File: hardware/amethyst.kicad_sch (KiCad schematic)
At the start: 0 parts

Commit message: Layout done
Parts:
- added C1, C2: C, Capacitor_SMD:C_0402_1005Metric, symbol Device:C
- added C10, C11, C12, C13, C14, C3, C4, C5, C6, C7, C8: 100n, Capacitor_SMD:C_0402_1005Metric, symbol Device:C
- added C9: 1u, Capacitor_SMD:C_0402_1005Metric, symbol Device:C
- added J1: Conn_01x02_Pin, Connector_PinHeader_1.00mm:PinHeader_1x02_P1.00mm_Vertical, symbol Connector:Conn_01x02_Pin
- added J2: USB_C_Receptacle_USB2.0_16P, Connector_USB:USB_C_Receptacle_XKB_U262-16XN-4BVC11, symbol Connector:USB_C_Receptacle_USB2.0_16P
- added R1, R2: 5.1k, Resistor_SMD:R_0402_1005Metric, symbol Device:R
- added R3: 1k, Resistor_SMD:R_0402_1005Metric, symbol Device:R
- added R4, R5: 27, Resistor_SMD:R_0402_1005Metric, symbol Device:R
- added U1: RP2040, Package_DFN_QFN:QFN-56-1EP_7x7mm_P0.4mm_EP3.2x3.2mm, symbol MCU_RaspberryPi:RP2040
- added U2: W25Q128JVS, Package_SO:SOIC-8_5.3x5.3mm_P1.27mm, symbol Memory_Flash:W25Q128JVS
- added Y1: Crystal_GND24_Small, Crystal:Crystal_SMD_3225-4Pin_3.2x2.5mm, symbol Device:Crystal_GND24_Small
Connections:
- new net: C2.2, R3.1, Y1.3
- new net: R3.2, U1.21 (XOUT)
- new net: C1.2, U1.20 (XIN), Y1.1
- new net: R4.2, U1.47 (USB_DP)
- new net: J2.A5 (CC1), R2.1
- new net: J2.A4 (VBUS), J2.A9 (VBUS), J2.B4 (VBUS), J2.B9 (VBUS)
- new net: J2.B5 (CC2), R1.1
- new net: J1.1 (Pin_1), U1.26 (RUN)
- new net: R5.2, U1.46 (USB_DM)
- new net +3V3: C10.1, C11.1, C12.1, C13.1, C14.1, C3.1, C4.1, C5.1, C6.1, C7.1, C8.1, C9.1, U1.1 (IOVDD), U1.10 (IOVDD), U1.22 (IOVDD), U1.23 (DVDD), U1.33 (IOVDD), U1.42 (IOVDD), U1.43 (ADC_AVDD), U1.44 (VREG_IN), U1.45 (VREG_VOUT), U1.48 (USB_VDD), U1.49 (IOVDD), U1.50 (DVDD), U2.8 (VCC)
- new net D+: J2.A6 (D+), J2.B6 (D+), R4.1
- new net D-: J2.A7 (D-), J2.B7 (D-), R5.1
- new net GND: C1.1, C10.2, C11.2, C12.2, C13.2, C14.2, C2.1, C3.2, C4.2, C5.2, C6.2, C7.2, C8.2, C9.2, J1.2 (Pin_2), J2.A1 (GND), J2.A12 (GND), J2.B1 (GND), J2.B12 (GND), J2.S1 (SHIELD), R1.2, R2.2, U1.19 (TESTEN), U1.57 (GND), U2.4 (GND), Y1.2, Y1.4
- new net QSPI_SCLK: U1.52 (QSPI_SCLK), U2.6 (CLK)
- new net QSPI_SD0: U1.53 (QSPI_SD0), U2.5 (DI/IO_{0})
- new net QSPI_SD1: U1.55 (QSPI_SD1), U2.2 (DO/IO_{1})
- new net QSPI_SD2: U1.54 (QSPI_SD2), U2.3 (~{WP}/IO_{2})
- new net QSPI_SD3: U1.51 (QSPI_SD3), U2.7 (~{HOLD}/~{RESET}/IO_{3})
- new net QSPI_SS: U1.56 (QSPI_SS), U2.1 (~{CS})
- no-connect marks 0 -> 4

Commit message: PCB Routing
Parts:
- removed C13, C14: 100n, Capacitor_SMD:C_0402_1005Metric, symbol Device:C
- removed J1: Conn_01x02_Pin, Connector_PinHeader_1.00mm:PinHeader_1x02_P1.00mm_Vertical, symbol Connector:Conn_01x02_Pin
- removed R3: 1k, Resistor_SMD:R_0402_1005Metric, symbol Device:R
- removed R4, R5: 27, Resistor_SMD:R_0402_1005Metric, symbol Device:R
- removed U1: RP2040, Package_DFN_QFN:QFN-56-1EP_7x7mm_P0.4mm_EP3.2x3.2mm, symbol MCU_RaspberryPi:RP2040
- removed U2: W25Q128JVS, Package_SO:SOIC-8_5.3x5.3mm_P1.27mm, symbol Memory_Flash:W25Q128JVS
- added U1: nRF52840, Package_DFN_QFN:Nordic_AQFN-73-1EP_7x7mm_P0.5mm, symbol MCU_Nordic:nRF52840
- C10: value 100n -> 100p
- C11, C12: value 100n -> 4.7u
- C9: value 1u -> 100n
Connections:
- net +3V3 is gone; now on net GND: C10.1, C11.1, C12.1, C3.1, C4.1, C5.1, C6.1, C7.1, C8.1, C9.1
- net D+: now also U1.AD6 (D+)
- net D-: now also U1.AD4 (D-)
- net GND: now also U1.B7 (VSS), U1.EP (VSS), U1.F23 (VSS_PA); no longer C10.2, C11.2, C12.2, C3.2, C4.2, C5.2, C6.2, C7.2, C8.2, C9.2
- net at C2.2, Y1.3: now also U1.A23 (XC2)
- net at C1.2, Y1.1: now also U1.B24 (XC1)
- net VBUS: now reaches J2.A4 (VBUS), J2.A9 (VBUS), J2.B4 (VBUS), J2.B9 (VBUS)
- net VBUS: now also C12.2, C4.2, U1.AD2 (VBUS), U1.Y2 (VDDH)
- new net: C3.2, U1.C1 (DEC1)
- new net: C10.2, U1.D23 (DEC3)
- new net: C11.2, U1.AC5 (DECUSB)
- new net: C5.2, C6.2, C7.2, C8.2, C9.2, U1.A22 (VDD), U1.AD14 (VDD), U1.AD23 (VDD), U1.B1 (VDD), U1.W1 (VDD)
- no-connect marks 4 -> 3
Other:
- moved on the sheet: C1, C2, Y1

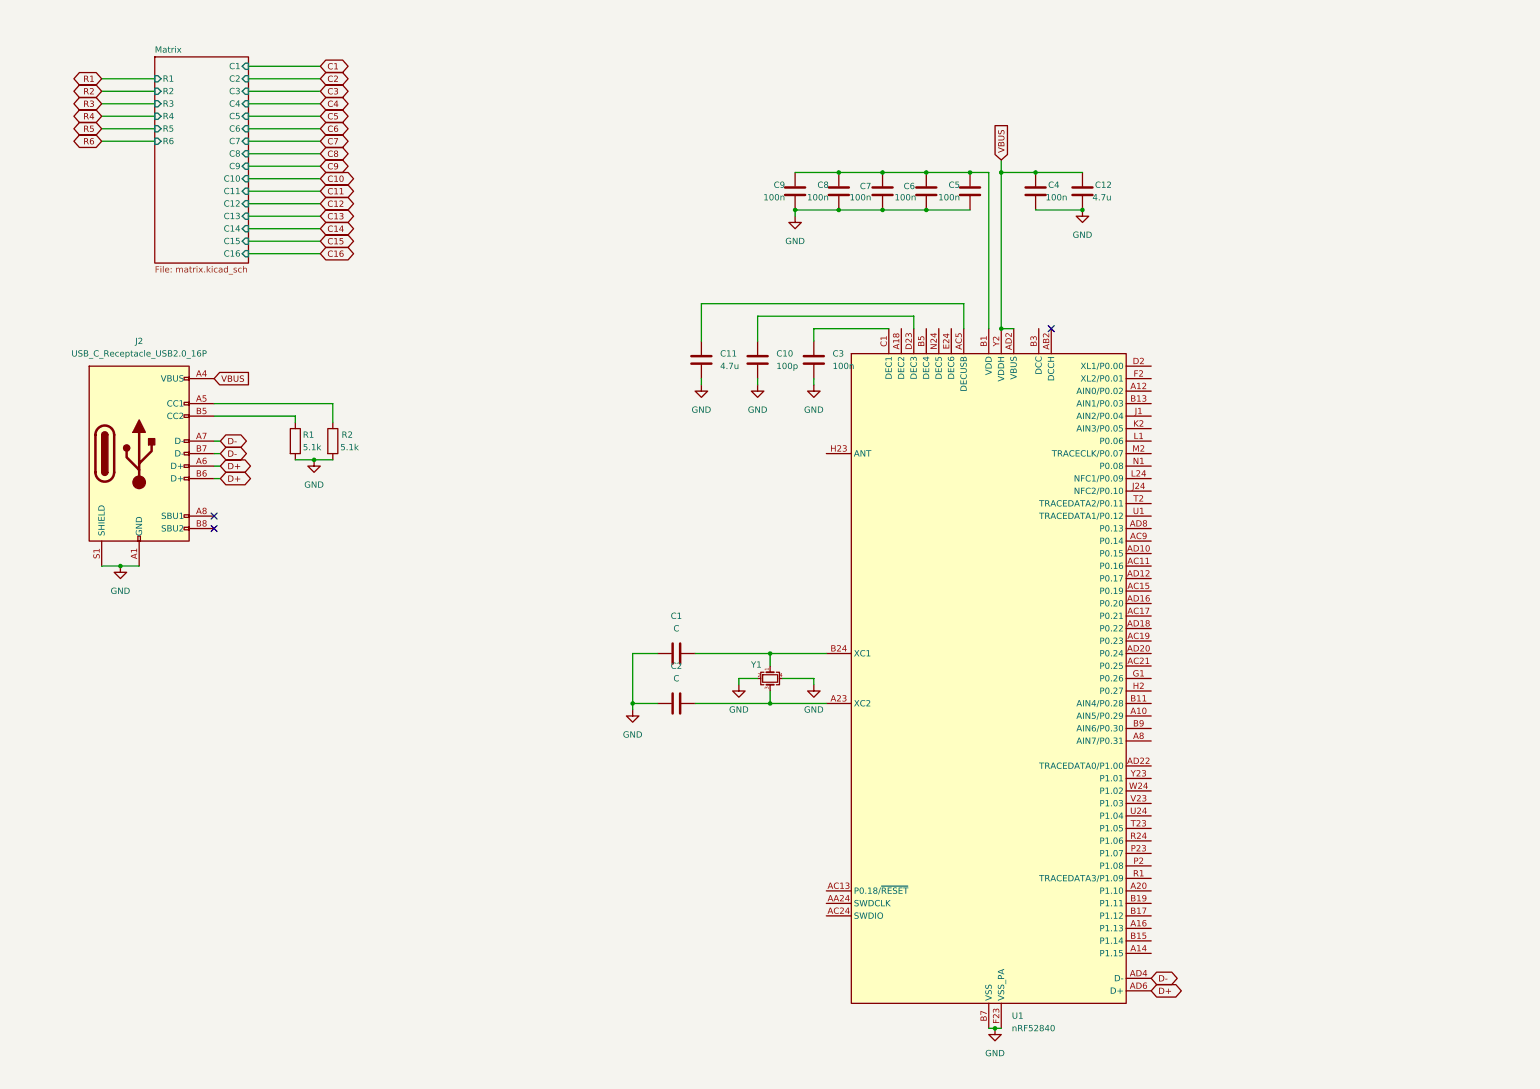
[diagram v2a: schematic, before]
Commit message: Power circuitry and nrf52840 circuitry
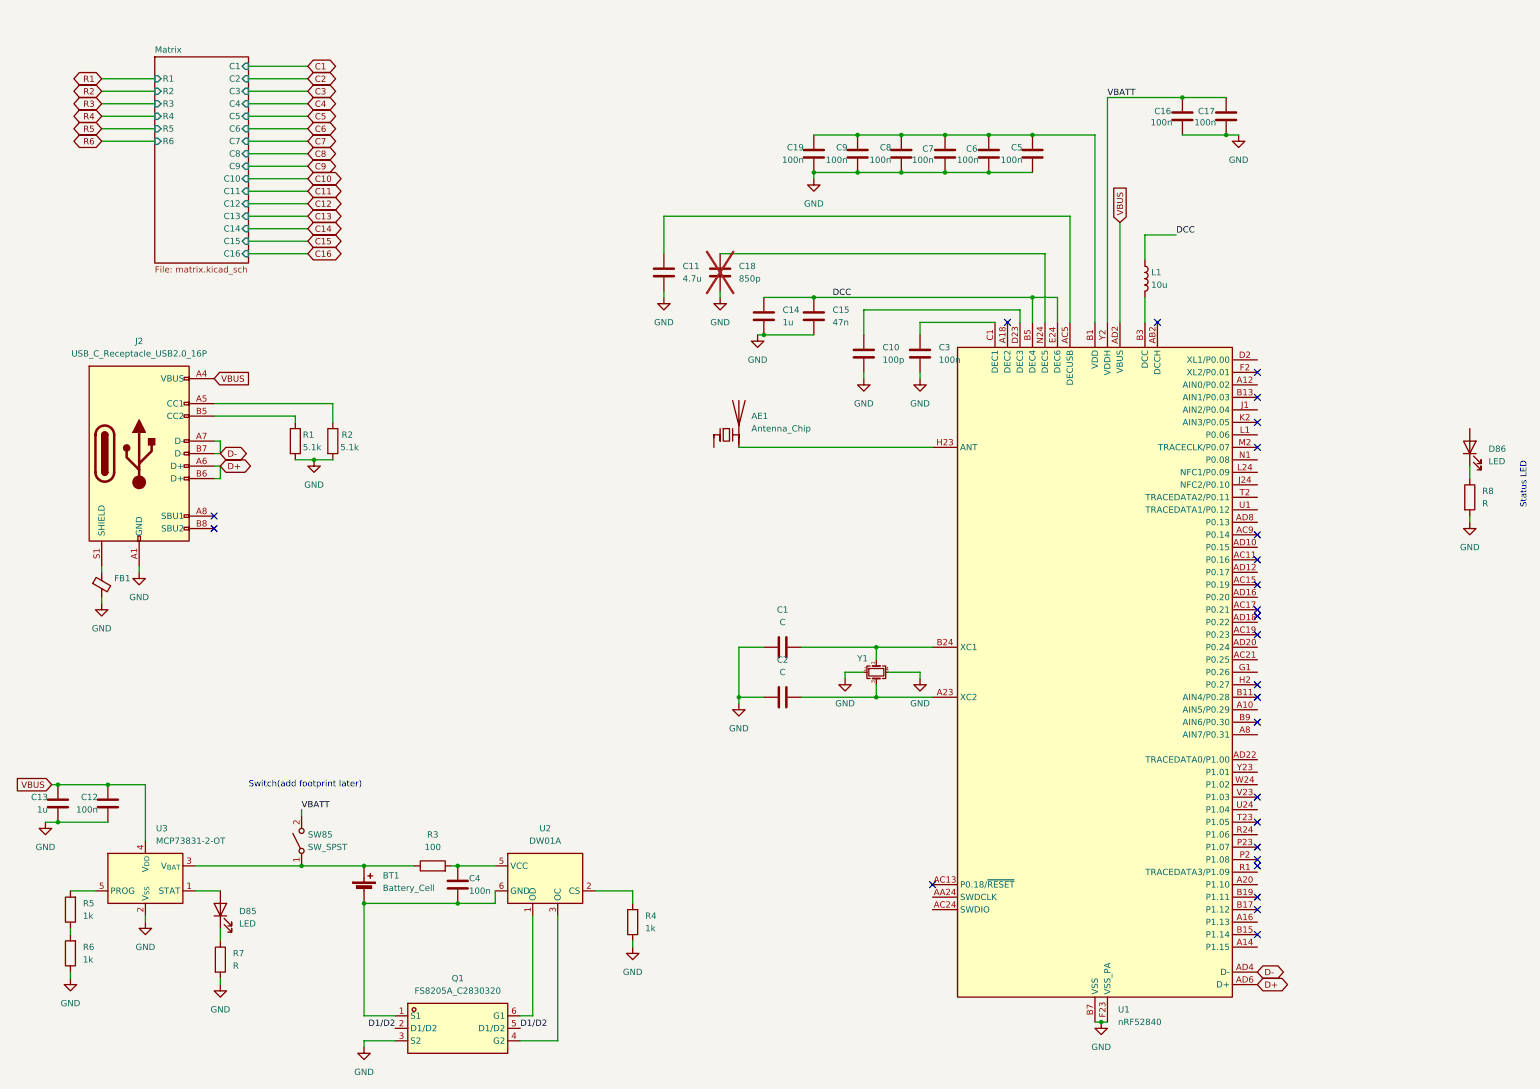
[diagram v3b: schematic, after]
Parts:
- added AE1: Antenna_Chip, symbol Device:Antenna_Chip
- added BT1: Battery_Cell, symbol Device:Battery_Cell
- added C13, C14: 1u, Capacitor_SMD:C_0402_1005Metric, symbol Device:C
- added C15: 47n, Capacitor_SMD:C_0402_1005Metric, symbol Device:C
- added C16, C17, C19: 100n, Capacitor_SMD:C_0402_1005Metric, symbol Device:C
- added C18: 850p, Capacitor_SMD:C_0402_1005Metric, symbol Device:C
- added D85, D86: LED, LED_SMD:LED_0402_1005Metric, symbol Device:LED
- added FB1: FerriteBead_Small, Resistor_SMD:R_0603_1608Metric, symbol Device:FerriteBead_Small
- added L1: 10u, symbol Device:L
- added Q1: FS8205A_C2830320, easyeda2kicad:SOT-23-6_L2.9-W1.6-P0.95-LS2.8-BR, symbol easyeda2kicad:FS8205A_C2830320
- added R3: 100, Resistor_SMD:R_0402_1005Metric, symbol Device:R
- added R4, R5, R6: 1k, Resistor_SMD:R_0402_1005Metric, symbol Device:R
- added R7, R8: R, Resistor_SMD:R_0402_1005Metric, symbol Device:R
- added SW85: SW_SPST, symbol Switch:SW_SPST
- added U2: DW01A, Package_TO_SOT_SMD:SOT-23-6, symbol Battery_Management:DW01A
- added U3: MCP73831-2-OT, Package_TO_SOT_SMD:SOT-23-5, symbol Battery_Management:MCP73831-2-OT
- C12: value 4.7u -> 100n
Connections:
- net GND: now also C13.1, C14.1, C15.1, C16.1, C17.1, C18.1, C19.1, FB1.2, Q1.3 (S2), R4.1, R6.1, R7.2, R8.2, U3.2 (V_{SS}); no longer C4.1, J2.S1 (SHIELD)
- net VBUS: now also C13.2, U3.4 (V_{DD}); no longer C4.2, U1.Y2 (VDDH)
- net at C5.2, C6.2, C7.2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: now also C19.2
- net at U1.B3 (DCC): now also L1.2
- net DCC: now reaches U1.B5 (DEC4)
- net DCC: now also U1.E24 (DEC6), C14.2, C15.2, L1.1
- net at U1.H23 (ANT): now also AE1.2 (PCB_Trace)
- net at U1.N24 (DEC5): now also C18.2
- new net: D86.1 (K), R8.1
- new net: FB1.1, J2.S1 (SHIELD)
- new net: BT1.2 (-), C4.2, Q1.1 (S1), U2.6 (GND)
- new net: Q1.4 (G2), U2.3 (OC)
- new net: Q1.6 (G1), U2.1 (OD)
- new net: C4.1, R3.2, U2.5 (VCC)
- new net: D85.2 (A), U3.1 (STAT)
- new net: BT1.1 (+), R3.1, SW85.1 (A), U3.3 (V_{BAT})
- new net: R5.2, U3.5 (PROG)
- new net: R4.2, U2.2 (CS)
- new net: R5.1, R6.2
- new net: D85.1 (K), R7.1
- new net D1/D2: Q1.2 (D1/D2), Q1.5 (D1/D2)
- new net VBATT: C16.2, C17.2, SW85.2 (B), U1.Y2 (VDDH)
- no-connect marks 3 -> 26
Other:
- note added: "Status LED"
- note added: "Switch(add footprint later)"
- moved on the sheet: C1, C10, C11, C2, C3, C5, C6, C7, C8, C9, U1, Y1

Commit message: Routing
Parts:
- removed Q1: FS8205A_C2830320, easyeda2kicad:SOT-23-6_L2.9-W1.6-P0.95-LS2.8-BR, symbol easyeda2kicad:FS8205A_C2830320
- removed R7: R, Resistor_SMD:R_0402_1005Metric, symbol Device:R
- removed U2: DW01A, Package_TO_SOT_SMD:SOT-23-6, symbol Battery_Management:DW01A
- removed U3: MCP73831-2-OT, Package_TO_SOT_SMD:SOT-23-5, symbol Battery_Management:MCP73831-2-OT
- added C20: 10u, Capacitor_SMD:C_0805_2012Metric, symbol Device:C
- added C21: 100n, Capacitor_SMD:C_0402_1005Metric, symbol Device:C
- added C22, C23: 1u, Capacitor_SMD:C_0402_1005Metric, symbol Device:C
- added U2: BQ25185DLHR, Package_DFN_QFN:Texas_DLH0010A_WSON-10-1EP_2.2x2mm_P0.4mm_EP0.9x1.5mm_ThermalVias, symbol easyeda2kicad:BQ25185DLHR
- BT1: footprint (none) -> Connector_JST:JST_EH_B2B-EH-A_1x02_P2.50mm_Vertical
- C13: value 1u -> 10u; footprint Capacitor_SMD:C_0402_1005Metric -> Capacitor_SMD:C_0805_2012Metric
- C4: value 100n -> 1u
- R3: value 100 -> 1k
- R4: value 1k -> 18k
- R5: value 1k -> 10k
- R6: value 1k -> R
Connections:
- net VBATT is gone; now on net VSYS: C16.2, C17.2, SW85.2 (B), U1.Y2 (VDDH)
- net GND: now also BT1.2 (-), C13.2, C4.1, R3.2, R4.2, R5.2, C20.2, C21.1, C22.1, C23.1, U2.11 (EP), U2.4 (~{CE}), U2.5 (GND); no longer C13.1, R4.1, R6.1
- net VBUS: now also C13.1, C4.2, U2.10 (IN); no longer C13.2
- net VSYS: now reaches D85.2 (A)
- net at R6.2: now also D85.1 (K); no longer R5.1
- new net: C20.1, C21.2, C22.2, SW85.1 (A), U2.1 (SYS)
- new net: R6.1, U2.3 (STAT2)
- new net: BT1.1 (+), C23.2, U2.2 (BAT)
- new net: R5.1, U2.6 (TS/MR)
- new net: R4.1, U2.7 (ILIM/VSET)
- new net: R3.1, U2.8 (ISET)
- no-connect marks 26 -> 27
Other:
- moved on the sheet: BT1, SW85

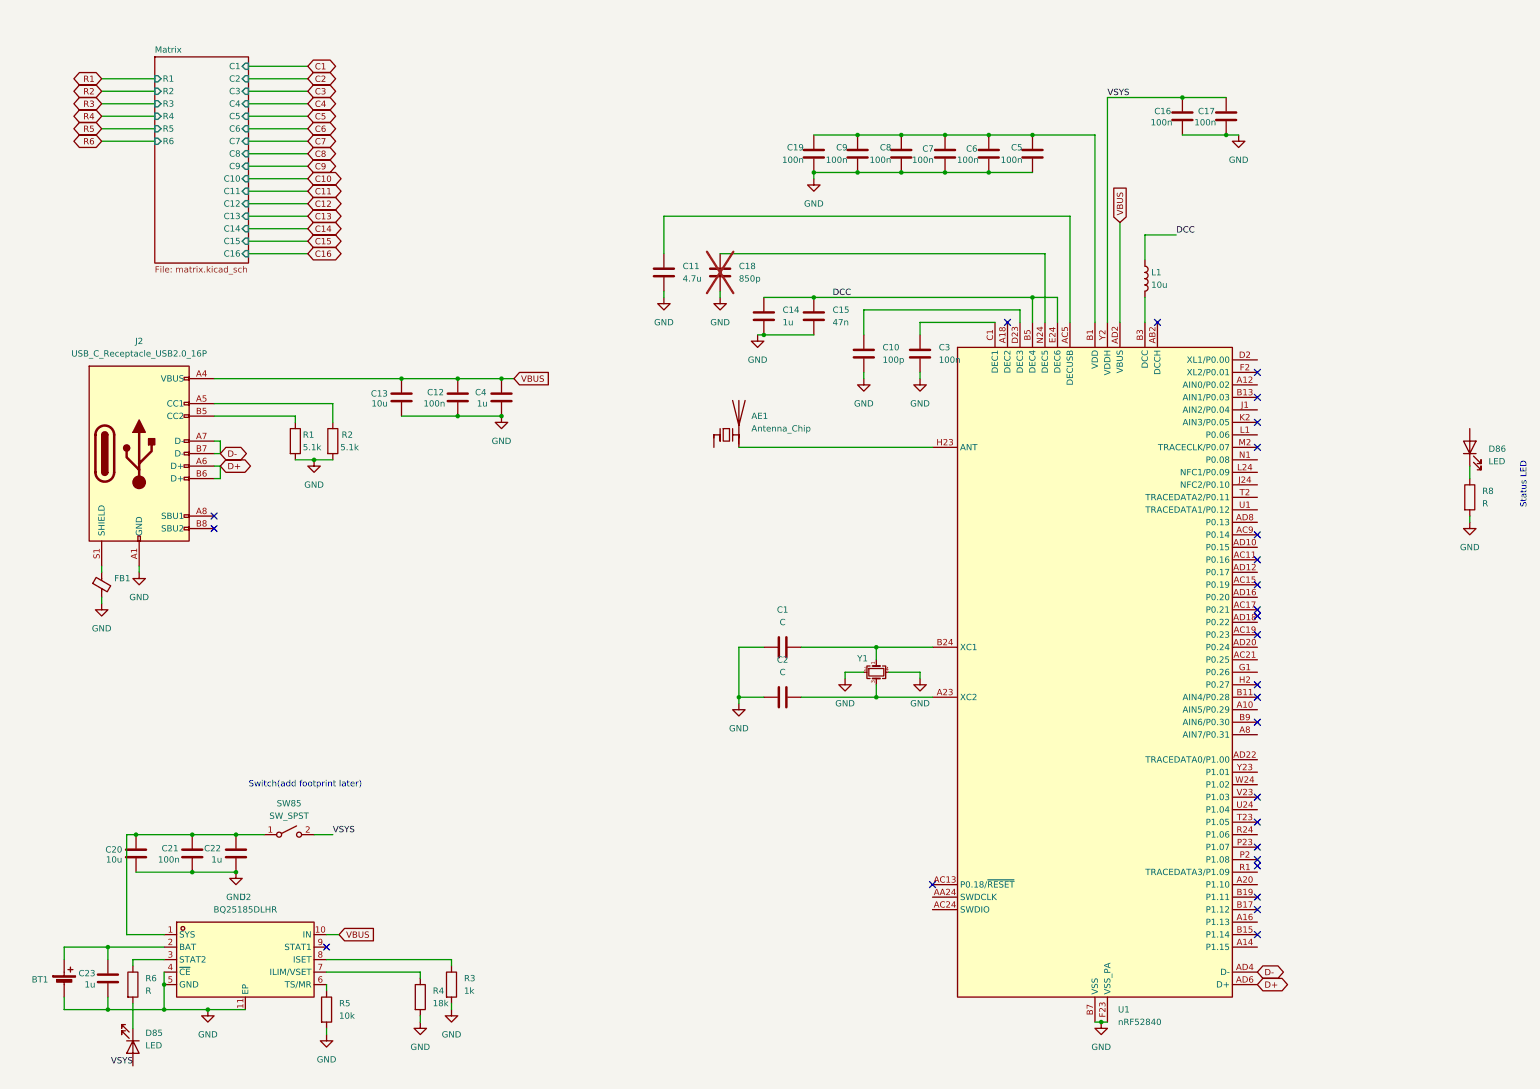
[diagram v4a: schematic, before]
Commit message: Matrix Routing and antenna placement
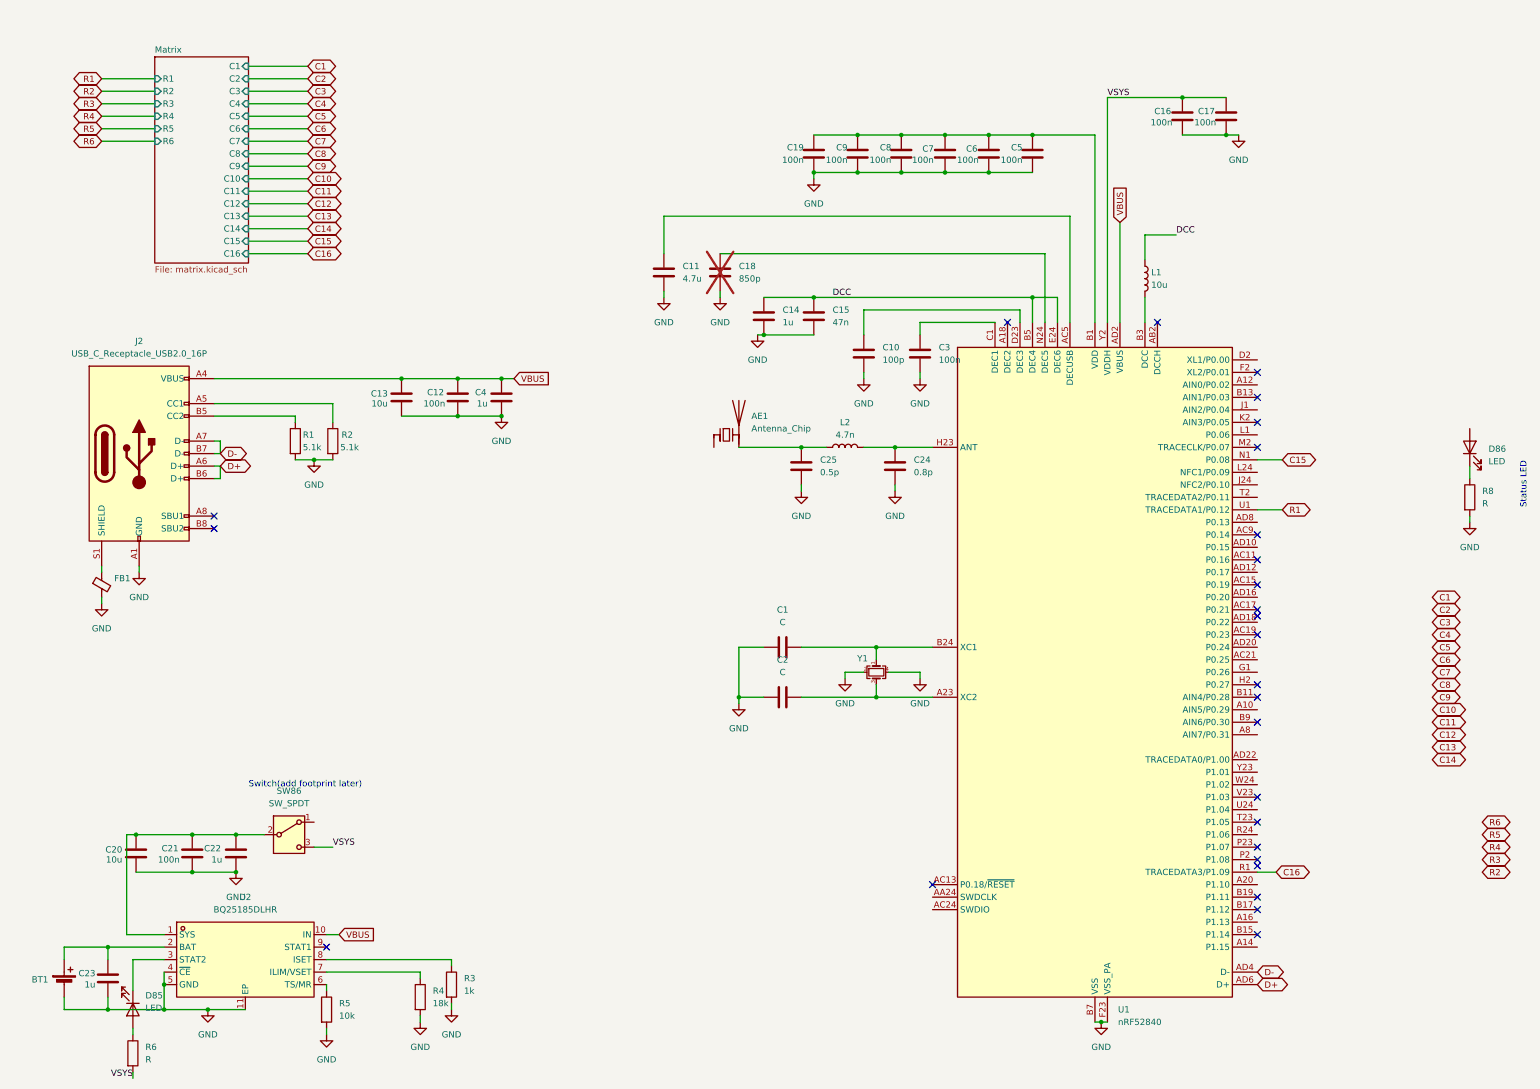
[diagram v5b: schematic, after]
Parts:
- removed SW85: SW_SPST, symbol Switch:SW_SPST
- added C24: 0.8p, symbol Device:C
- added C25: 0.5p, symbol Device:C
- added L2: 4.7n, symbol Device:L
- added SW86: SW_SPDT, symbol Switch:SW_SPDT
- AE1: footprint (none) -> RF_Antenna:Johanson_2450AT18x100
- L1: footprint (none) -> Inductor_SMD:L_smd_1212_3232metric
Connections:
- net C15: now also U1.N1 (P0.08)
- net C16: now also U1.R1 (TRACEDATA3/P1.09)
- net GND: now also C24.2, C25.2
- net R1: now also U1.U1 (TRACEDATA1/P0.12)
- net VSYS: now also R6.2, SW86.3 (C); no longer D85.2 (A)
- net at C20.1, C21.2, C22.2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: now also SW86.2 (B)
- net at D85.1 (K): now also U2.3 (STAT2); no longer R6.2
- net at R6.1: now also D85.2 (A); no longer U2.3 (STAT2)
- net at U1.H23 (ANT): now also C24.1, L2.2; no longer AE1.2 (PCB_Trace)
- new net: AE1.2 (PCB_Trace), C25.1, L2.1
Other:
- moved on the sheet: D85, R6

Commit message: matrix routing
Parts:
- removed FB1: FerriteBead_Small, Resistor_SMD:R_0603_1608Metric, symbol Device:FerriteBead_Small
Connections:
- net C10: now also U1.AD12 (P0.17)
- net C11: now also U1.AD10 (P0.15)
- net C12: now also U1.AD8 (P0.13)
- net C13: now also U1.J1 (AIN2/P0.04)
- net C14: now also U1.L1 (P0.06)
- net C3: now also U1.A12 (AIN0/P0.02)
- net C4: now also U1.A10 (AIN5/P0.29)
- net C5: now also U1.AC21 (P0.25)
- net C6: now also U1.AD22 (TRACEDATA0/P1.00)
- net C7: now also U1.AD20 (P0.24)
- net C8: now also U1.AD18 (P0.22)
- net C9: now also U1.AD16 (P0.20)
- net R2: now also U1.G1 (P0.26)
- net R3: now also U1.A8 (AIN7/P0.31)
- no-connect marks 27 -> 28
